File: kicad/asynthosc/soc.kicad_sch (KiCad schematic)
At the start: 47 parts, among them J11 Conn_01x04_Pin, J6 Conn_01x04_Pin, J9 Conn_01x07_Pin, SW2 SW_Push, U10 W25Q32JVSS, U2 STM32H723ZGTx, Y1 8MHz, 8pF

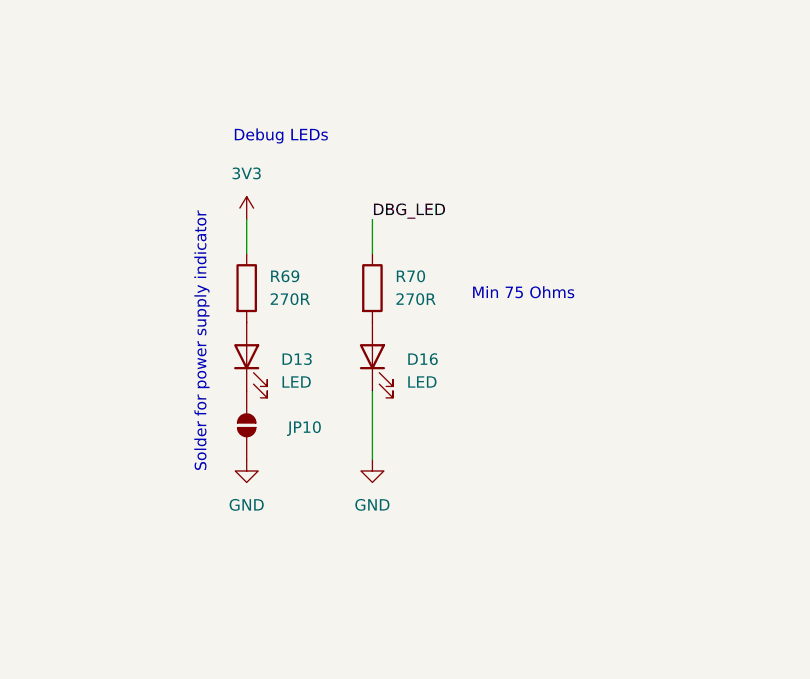
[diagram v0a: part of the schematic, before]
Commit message: sch: update footprint links
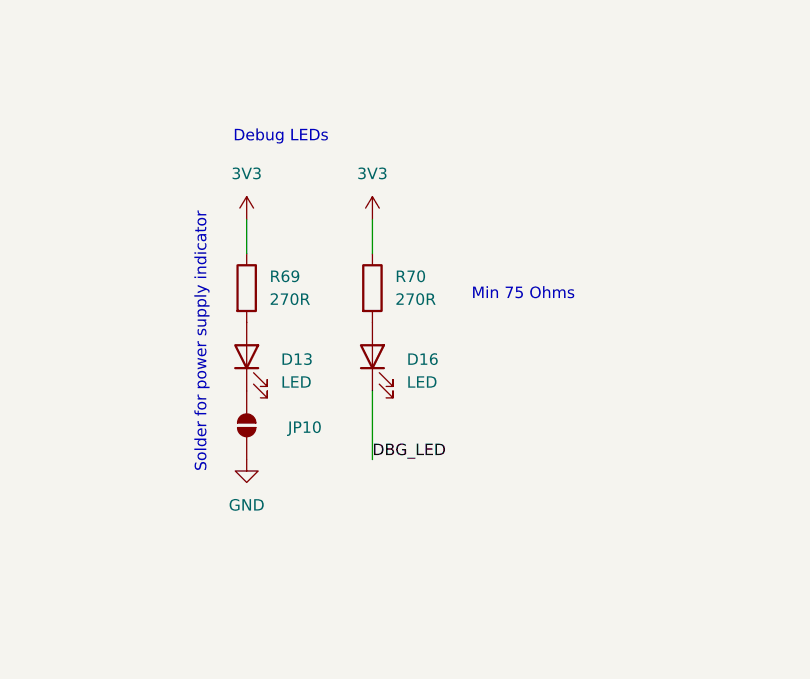
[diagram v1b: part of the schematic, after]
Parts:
- C11, C29, C7: footprint (none) -> Capacitor_SMD:C_0805_2012Metric
- C16, C17, C18, C19, C20, C21, C22, C23, C24, C25, C26, C27, C28, C30, C51: footprint (none) -> Capacitor_SMD:C_0402_1005Metric
- D13, D16: footprint 0402 -> LED_SMD:LED_0402_1005Metric
- J11, J9, R15, R16, R17, R18, R19, R20, R33, R34, R61, R7, R8: footprint (none) -> Resistor_SMD:R_0402_1005Metric
- J6: footprint (none) -> Connector_PinHeader_2.54mm:PinHeader_1x04_P2.54mm_Vertical
- JP1, JP2, JP3, JP5, JP6: footprint (none) -> Jumper:SolderJumper-2_P1.3mm_Bridged2Bar_Pad1.0x1.5mm
- JP10: footprint (none) -> Jumper:SolderJumper-2_P1.3mm_Open_Pad1.0x1.5mm
- R69, R70: footprint 0402 -> Resistor_SMD:R_0402_1005Metric
- Y1: footprint (none) -> Crystal:Crystal_SMD_3225-4Pin_3.2x2.5mm; RefNum NX3225GD-8MHz-EXS00A-CG04874 -> (none)
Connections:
- net 3V3: now also R70.1
- net DBG_LED: now also D16.1 (K); no longer R70.1
- net GND: no longer D16.1 (K)

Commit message: wip
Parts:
- removed J11: Conn_01x04_Pin, Resistor_SMD:R_0402_1005Metric, symbol Connector:Conn_01x04_Pin
- removed J6: Conn_01x04_Pin, Connector_PinHeader_2.54mm:PinHeader_1x04_P2.54mm_Vertical, symbol Connector:Conn_01x04_Pin
- removed J9: Conn_01x07_Pin, Resistor_SMD:R_0402_1005Metric, symbol Connector:Conn_01x07_Pin
- added J10: Conn_02x07_Odd_Even, Connector_PinSocket_2.54mm:PinSocket_2x07_P2.54mm_Vertical_SMD, symbol Connector_Generic:Conn_02x07_Odd_Even
- added J12: Conn_02x04_Odd_Even, Connector_PinHeader_2.54mm:PinHeader_2x04_P2.54mm_Vertical_SMD, symbol Connector_Generic:Conn_02x04_Odd_Even
- added J9: Conn_ARM_SWD_TagConnect_TC2030-NL, Connector:Tag-Connect_TC2030-IDC-NL_2x03_P1.27mm_Vertical, symbol Connector:Conn_ARM_SWD_TagConnect_TC2030-NL
- FB2: footprint (none) -> Inductor_SMD:L_0402_1005Metric
- SW2: footprint (none) -> Button_Switch_SMD:SW_SPST_B3S-1000; RefNum (none) -> Boomele 6.0*6.0*6.0; now not fitted
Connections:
- net 3V3: now also J10.2 (Pin_2), J9.1 (VCC)
- net GND: now also J10.1 (Pin_1), J10.11 (Pin_11), J10.13 (Pin_13), J10.3 (Pin_3), J10.5 (Pin_5), J10.6 (Pin_6), J10.7 (Pin_7), J10.9 (Pin_9), J12.4 (Pin_4), J12.5 (Pin_5), J9.5 (GND)
- net at R20.1: now also J12.7 (Pin_7)
- net at R33.1: now also J12.1 (Pin_1)
- net JTMS_CONN: now reaches R15.1
- net JTMS_CONN: now also J10.8 (Pin_8), J9.2 (SWDIO)
- net at R18.1: now also J12.2 (Pin_2)
- net JTDI_CONN: now reaches R7.1
- net JTDI_CONN: now also J10.14 (Pin_14)
- net JTDO_CONN: now reaches R17.1
- net JTDO_CONN: now also J10.12 (Pin_12), J9.6 (SWO)
- net JTCK_CONN: now reaches R8.1
- net JTCK_CONN: now also J10.4 (Pin_4), J9.4 (SWCLK)
- net at R19.1: now also J12.8 (Pin_8)
- net NRST_CONN: now reaches R16.1
- net NRST_CONN: now also J10.10 (Pin_10), J9.3 (~{RESET})
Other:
- note added: "TagConnect 2050"
- moved on the sheet: R15, R16, R17, R20, R33, R7, R8

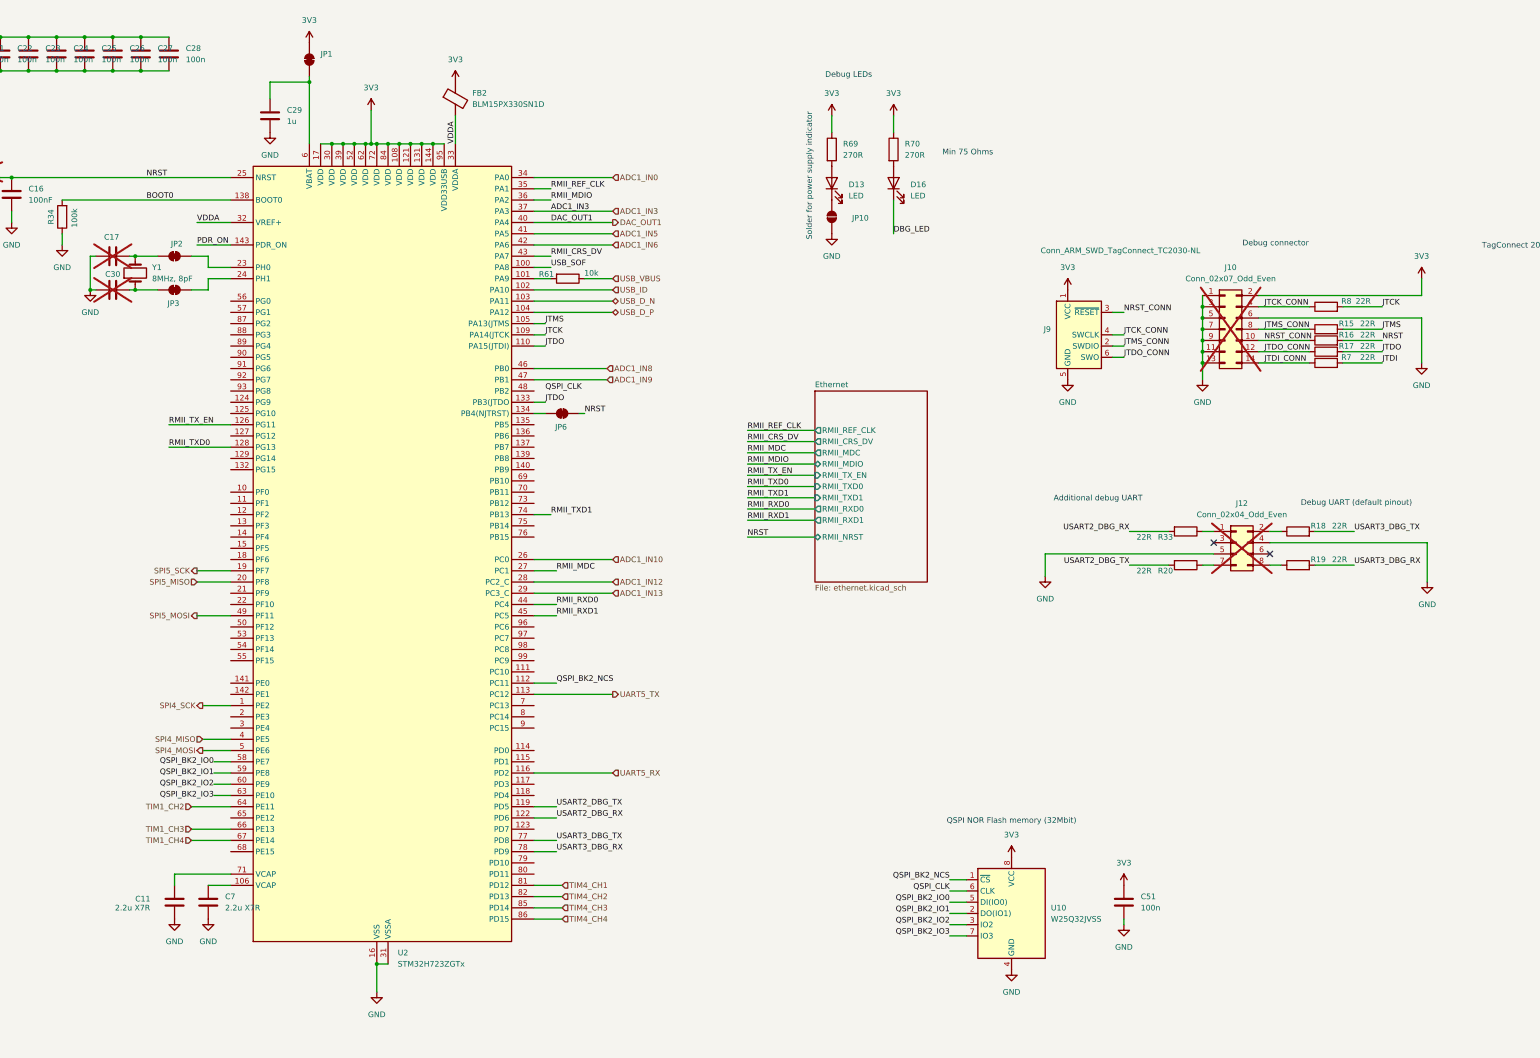
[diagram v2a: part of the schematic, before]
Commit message: sch: change stm32 for smaller one, create smaller jumper footprint
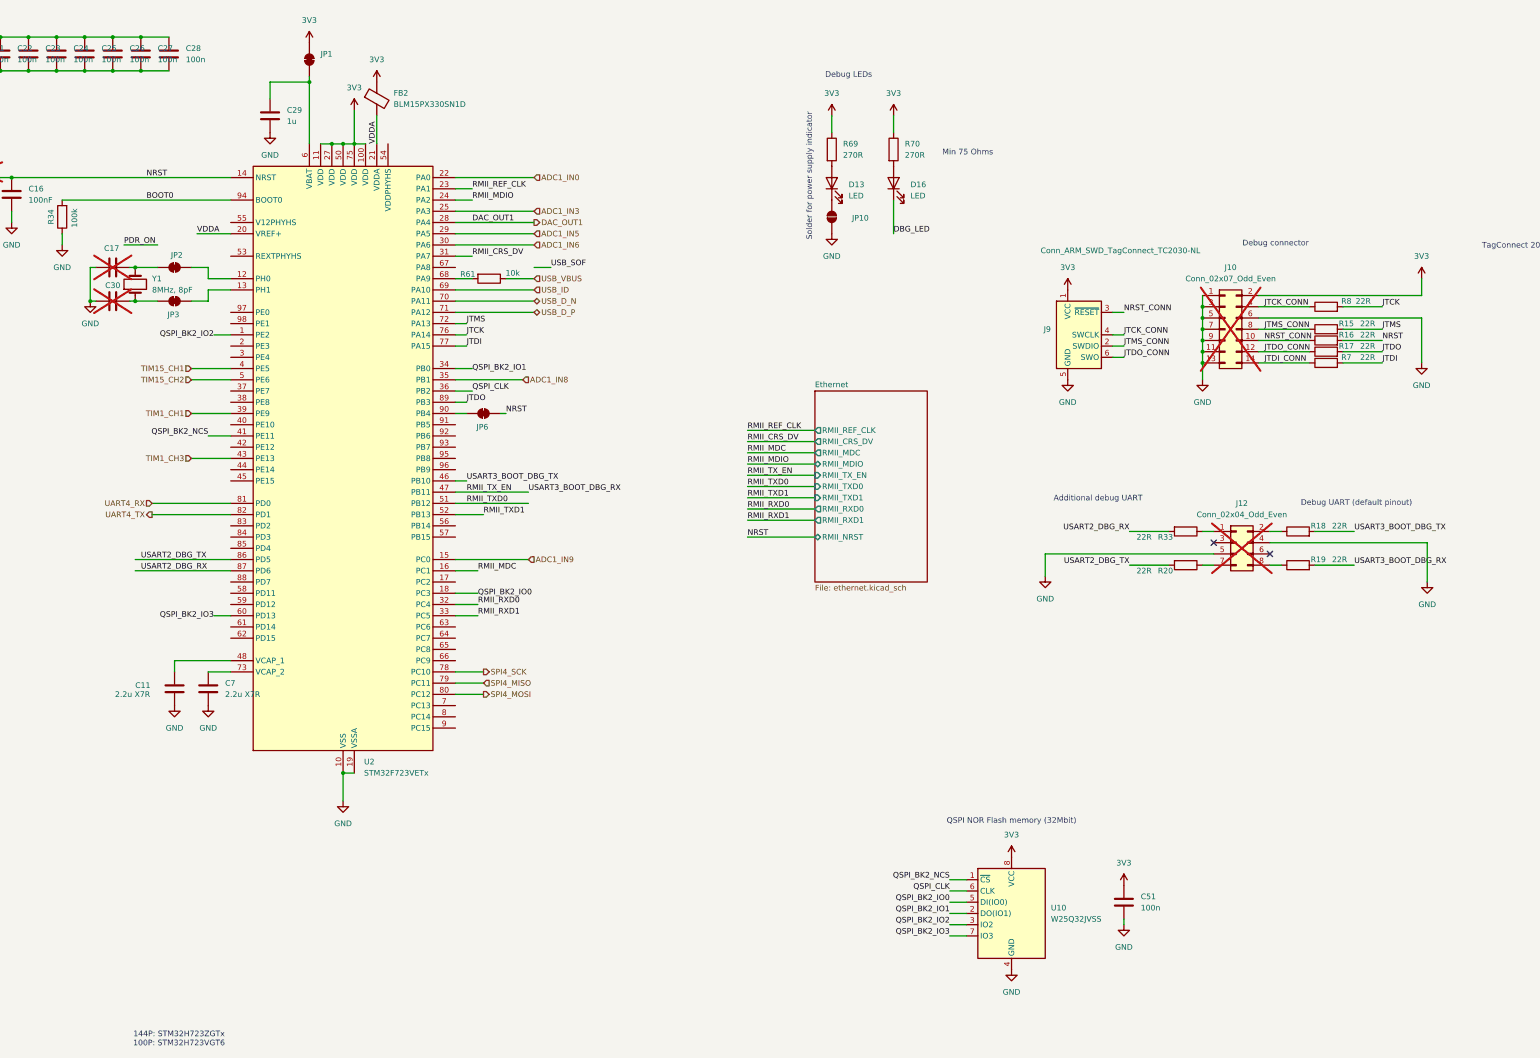
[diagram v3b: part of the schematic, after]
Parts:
- removed U2: STM32H723ZGTx, Package_QFP:LQFP-144_20x20mm_P0.5mm, symbol MCU_ST_STM32H7:STM32H723ZGTx
- added U2: STM32F723VETx, Package_QFP:LQFP-100_14x14mm_P0.5mm, symbol MCU_ST_STM32F7:STM32F723VETx
- C11, C16, C17, C18, C19, C20, C21, C22, C23, C24, C25, C26, C27, C28, C29, C30, C51, C7, D13, D16: RefNum (none) -> _generic_
- FB2: Manufacturer (none) -> Murata; RefNum (none) -> BLM15PX330SN1D
- JP1, JP2, JP3, JP5, JP6: footprint Jumper:SolderJumper-2_P1.3mm_Bridged2Bar_Pad1.0x1.5mm -> asynthosc:SolderJumper_0402_1005Metric_Bridged
- JP10: footprint Jumper:SolderJumper-2_P1.3mm_Open_Pad1.0x1.5mm -> Resistor_SMD:R_0402_1005Metric
- SW2: Manufacturer (none) -> Boomele; RefNum Boomele 6.0*6.0*6.0 -> 6.0*6.0*6.0
- U10: Manufacturer (none) -> Winbond; RefNum (none) -> W25Q32JVSS
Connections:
- net USART3_DBG_RX is gone; now on net RMII_TX_EN: R19.2
- net 3V3: now also U2.100 (VDD), U2.11 (VDD), U2.27 (VDD), U2.50 (VDD), U2.75 (VDD)
- net ADC1_IN0: now also U2.22 (PA0)
- net ADC1_IN3: now also U2.25 (PA3)
- net ADC1_IN5: now also U2.29 (PA5)
- net ADC1_IN6: now also U2.30 (PA6)
- net ADC1_IN8: now also U2.35 (PB1)
- net ADC1_IN9: now also U2.15 (PC0)
- net BOOT0: now also U2.94 (BOOT0)
- net DAC_OUT1: now also U2.28 (PA4)
- net GND: now also U2.10 (VSS), U2.19 (VSSA), U2.26 (VSS), U2.49 (VSS), U2.74 (VSS), U2.99 (VSS)
- net JTCK: now also U2.76 (PA14)
- net JTDI: now also U2.77 (PA15)
- net JTDO: now also U2.89 (PB3)
- net JTMS: now also U2.72 (PA13)
- net NRST: now also U2.14 (NRST)
- net QSPI_BK2_IO0: now also U2.18 (PC3)
- net QSPI_BK2_IO1: now also U2.34 (PB0)
- net QSPI_BK2_IO2: now also U2.1 (PE2)
- net QSPI_BK2_IO3: now also U2.60 (PD13)
- net QSPI_BK2_NCS: now also U2.41 (PE11)
- net QSPI_CLK: now also U2.36 (PB2)
- net RMII_CRS_DV: now also U2.31 (PA7)
- net RMII_MDC: now also U2.16 (PC1)
- net RMII_MDIO: now also U2.24 (PA2)
- net RMII_REF_CLK: now also U2.23 (PA1)
- net RMII_RXD0: now also U2.32 (PC4)
- net RMII_RXD1: now also U2.33 (PC5)
- net RMII_TXD0: now also U2.51 (PB12)
- net RMII_TXD1: now also U2.52 (PB13)
- net RMII_TX_EN: now also U2.47 (PB11)
- net SPI4_MISO: now also U2.79 (PC11)
- net SPI4_MOSI: now also U2.80 (PC12)
- net SPI4_SCK: now also U2.78 (PC10)
- net TIM1_CH3: now also U2.43 (PE13)
- net USART2_DBG_RX: now also U2.87 (PD6)
- net USART2_DBG_TX: now also U2.86 (PD5)
- net USB_D_N: now also U2.70 (PA11)
- net USB_D_P: now also U2.71 (PA12)
- net USB_ID: now also U2.69 (PA10)
- net VDDA: now also U2.20 (VREF+), U2.21 (VDDA)
- net at JP3.1 (A): now also U2.13 (PH1)
- net at JP2.1 (A): now also U2.12 (PH0)
- net at C29.1, JP1.1 (A): now also U2.6 (VBAT)
- net at C7.1: now also U2.73 (VCAP_2)
- net at R61.2: now also U2.68 (PA9)
- net at JP6.2 (B): now also U2.90 (PB4)
- net at C11.1: now also U2.48 (VCAP_1)
- net USART3_DBG_TX renamed USART3_BOOT_DBG_TX
- net USART3_BOOT_DBG_TX: now also U2.46 (PB10)
- new net TIM15_CH1: U2.4 (PE5)
- new net TIM15_CH2: U2.5 (PE6)
- new net TIM1_CH1: U2.39 (PE9)
- new net UART4_RX: U2.81 (PD0)
- new net UART4_TX: U2.82 (PD1)
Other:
- note added: "144P: STM32H723ZGTx 100P: STM32H723VGT6"
- moved on the sheet: C11, C17, C30, C7, FB2, JP2, JP3, JP6, R61, Y1
